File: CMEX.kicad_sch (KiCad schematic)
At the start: 8 parts, among them U1 DAC63004RTET, U2 TPS62151, U3 ADS8584S, U4 TLV8802, U5 TLV8801, U6 LMC7660, U7 SN65MLVD047AD

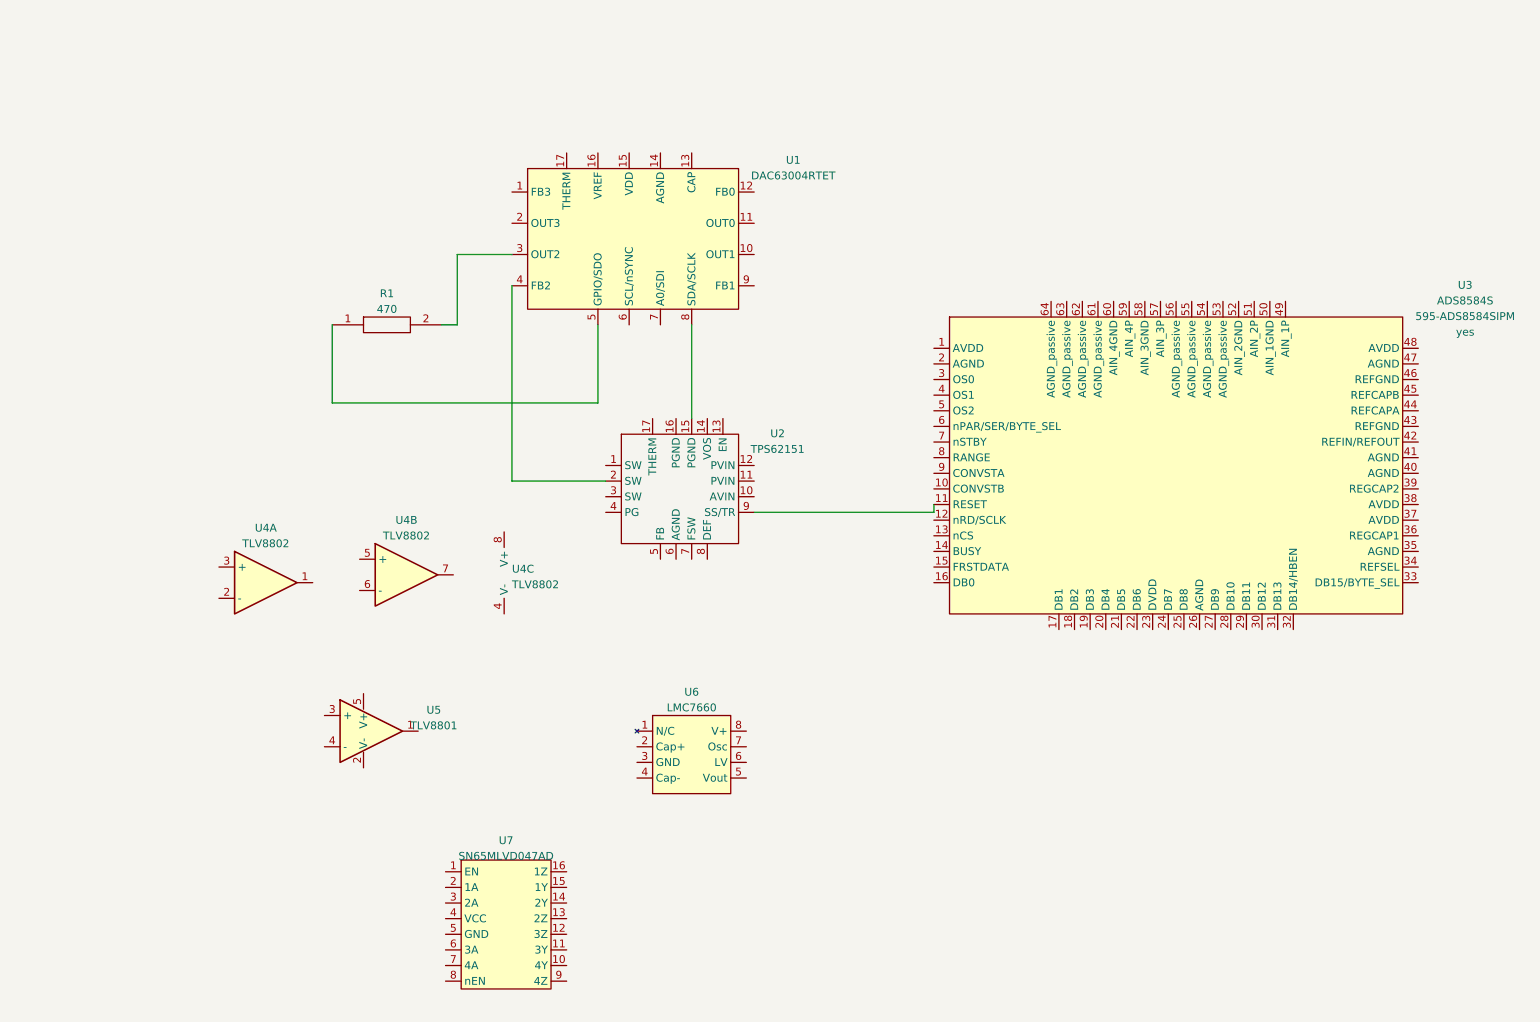
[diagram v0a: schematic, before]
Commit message: Added two sub-sheets for power supply and adc. Started to make the power supply.
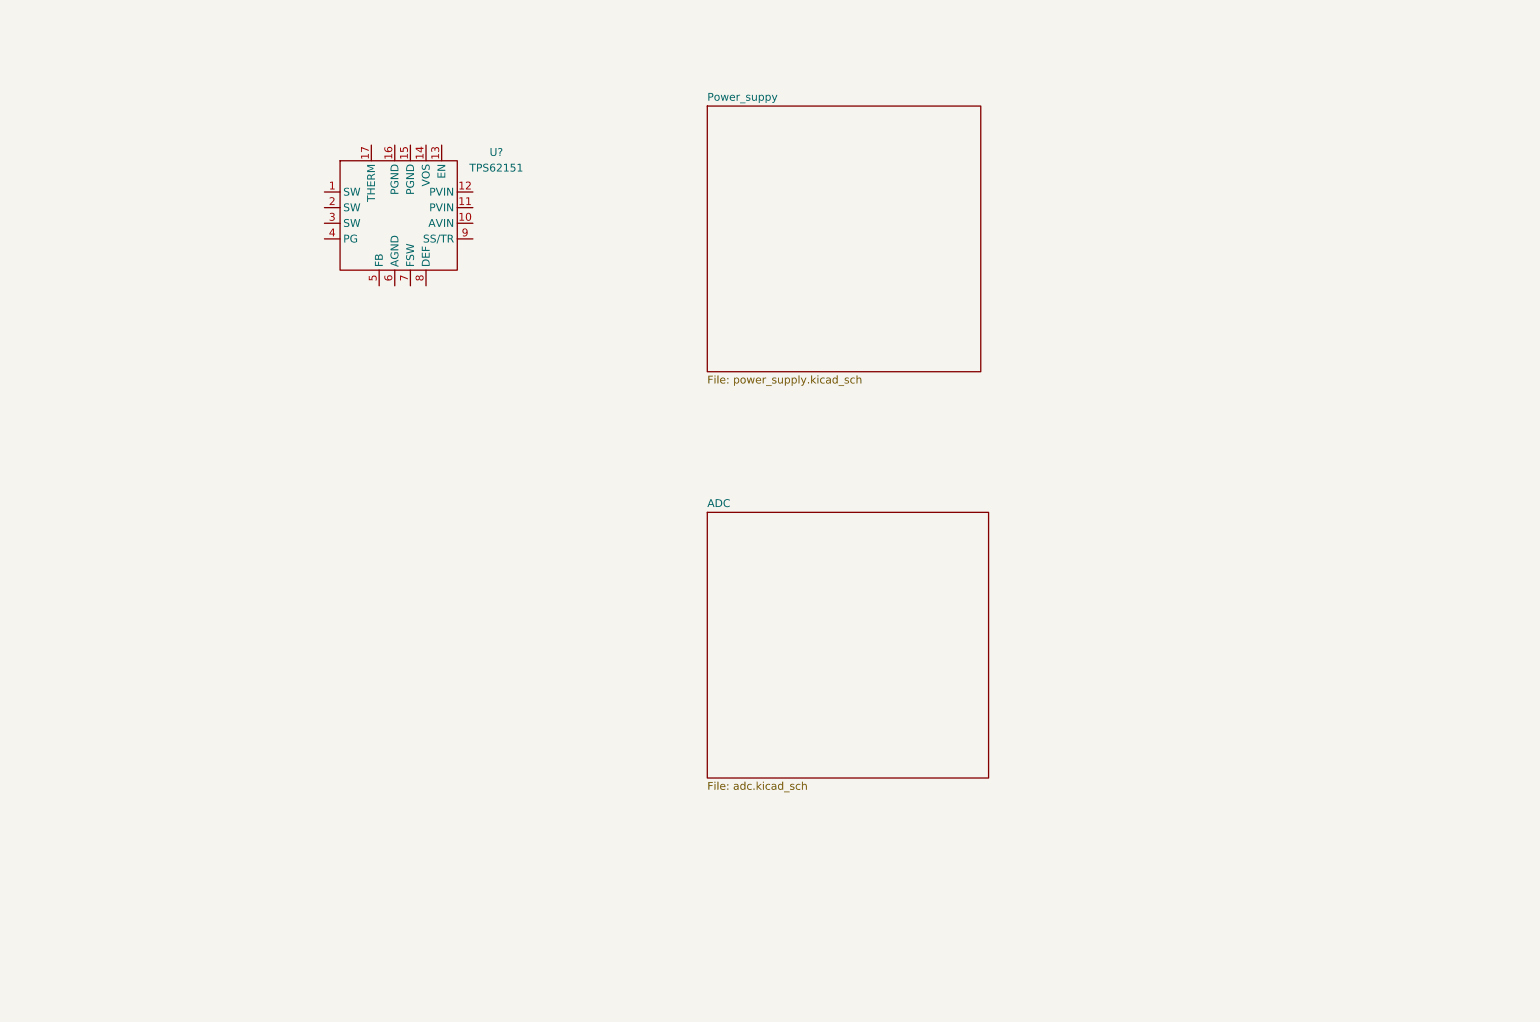
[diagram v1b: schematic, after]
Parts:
- removed R1: R0603_470, Resistor_SMD:R_0603_1608Metric, symbol Jojo_Kicad_Lib:R0603_470
- removed U1: DAC63004RTET, Package_DFN_QFN:WQFN-16-1EP_3x3mm_P0.5mm_EP1.68x1.68mm, symbol Jojo_Kicad_Lib:DAC63004RTET
- removed U2: TPS62151, Package_DFN_QFN:VQFN-16-1EP_3x3mm_P0.5mm_EP1.68x1.68mm, symbol Jojo_Kicad_Lib:TPS62151
- removed U3: ADS8584S, Package_QFP:LQFP-64_10x10mm_P0.5mm, symbol Jojo_Kicad_Lib:ADS8584S
- removed U4: TLV8802, Package_SO:VSSOP-8_3.0x3.0mm_P0.65mm, symbol Jojo_Kicad_Lib:TLV8802
- removed U5: TLV8801, Package_TO_SOT_SMD:SOT-23-5, symbol Jojo_Kicad_Lib:TLV8801
- removed U6: LMC7660, Package_SO:SOIC-8_3.9x4.9mm_P1.27mm, symbol Jojo_Kicad_Lib:LMC7660
- removed U7: SN65MLVD047AD, Package_SO:SOIC-16_3.9x9.9mm_P1.27mm, symbol Jojo_Kicad_Lib:SN65MLVD047AD
- added U?: TPS62151, Package_DFN_QFN:VQFN-16-1EP_3x3mm_P0.5mm_EP1.68x1.68mm, symbol Jojos_Lib:TPS62151
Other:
- added sheet ADC (adc.kicad_sch)
- added sheet Power_suppy (power_supply.kicad_sch)

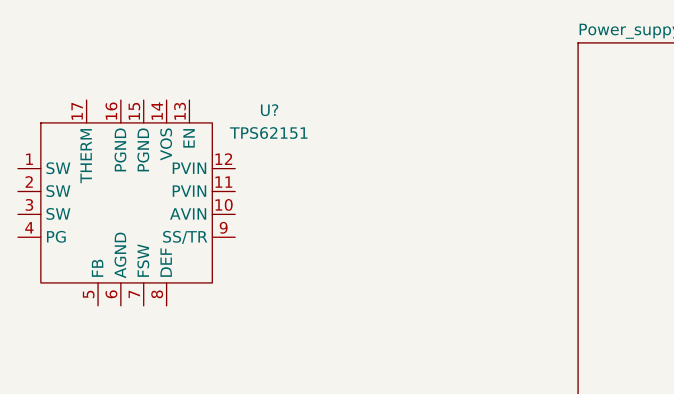
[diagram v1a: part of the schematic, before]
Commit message: Schaltplan für Spannungsversorgung angelegt.
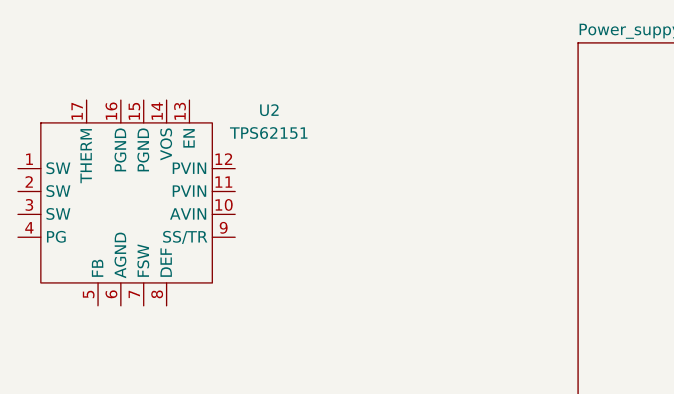
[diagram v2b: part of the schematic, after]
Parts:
- gave numbers to parts that had none: 1
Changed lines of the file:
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@@
   (symbol (lib_id "Jojos_Lib:TPS62151") (at 97.79 60.96 0) (unit 1)
     (in_bom yes) (on_board yes) (dnp no) (fields_autoplaced)
-    (property "Reference" "U?" (at 113.03 49.4283 0)
+    (property "Reference" "U2" (at 113.03 49.4283 0)
       (effects (font (size 1.27 1.27)))
     )
@@
       (project "CMEX"
         (path "/03c4a148-37f4-4d5a-ada3-efb0d725ba7b"
-          (reference "U?") (unit 1)
+          (reference "U2") (unit 1)
         )
       )

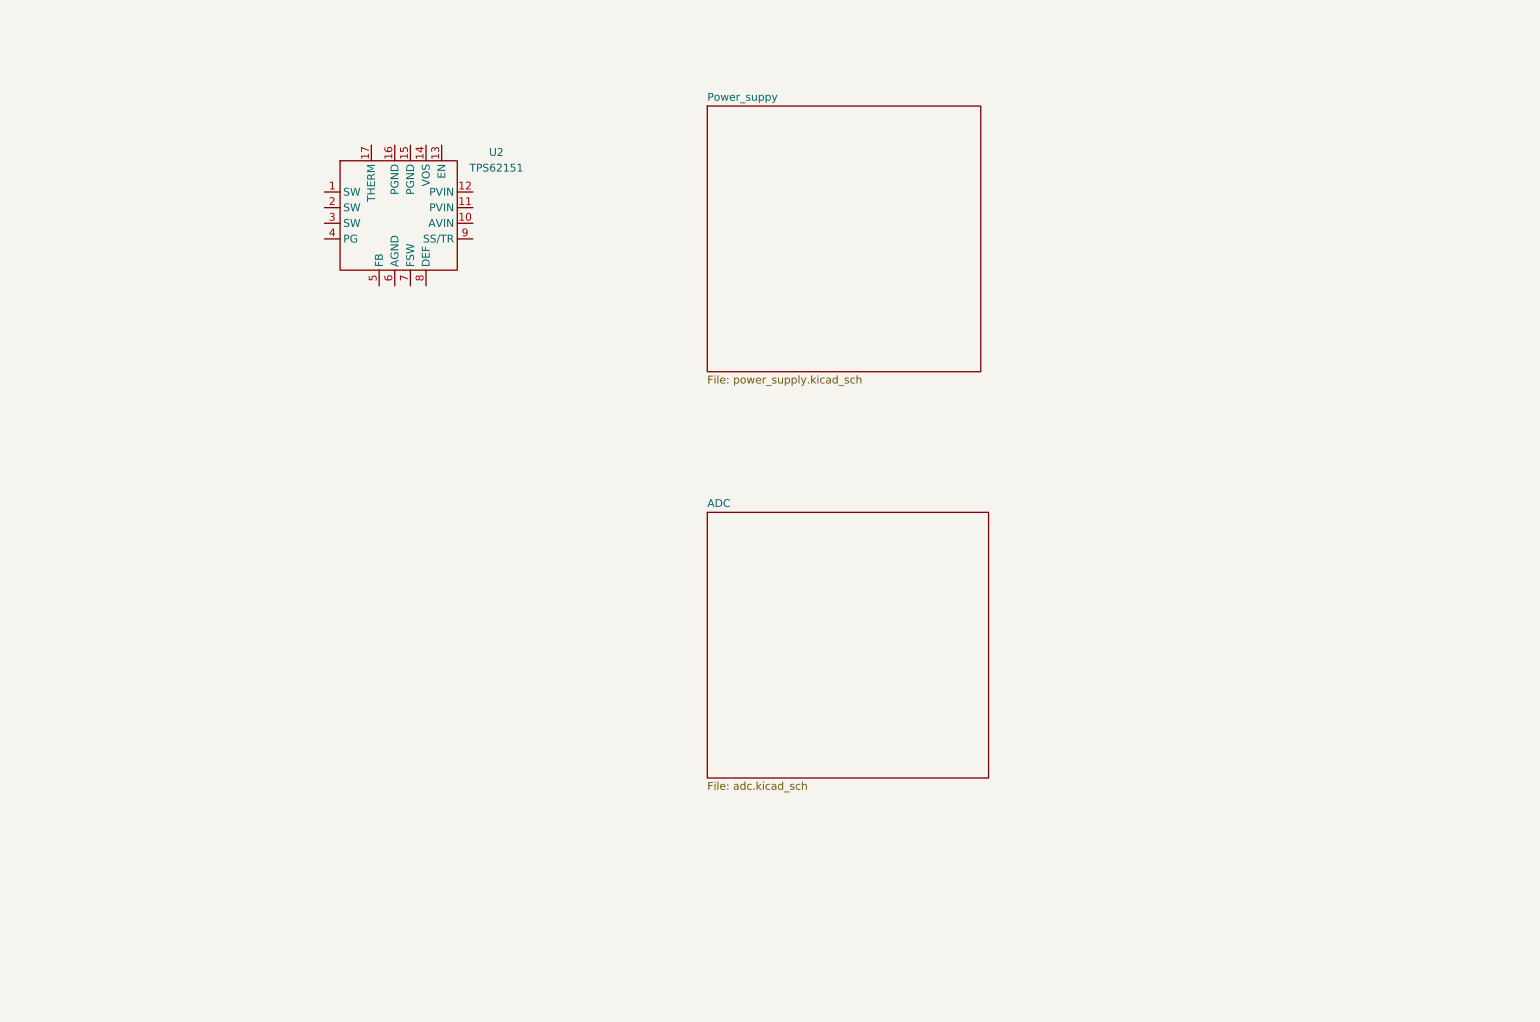
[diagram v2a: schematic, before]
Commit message: Added awags and dac sheet.
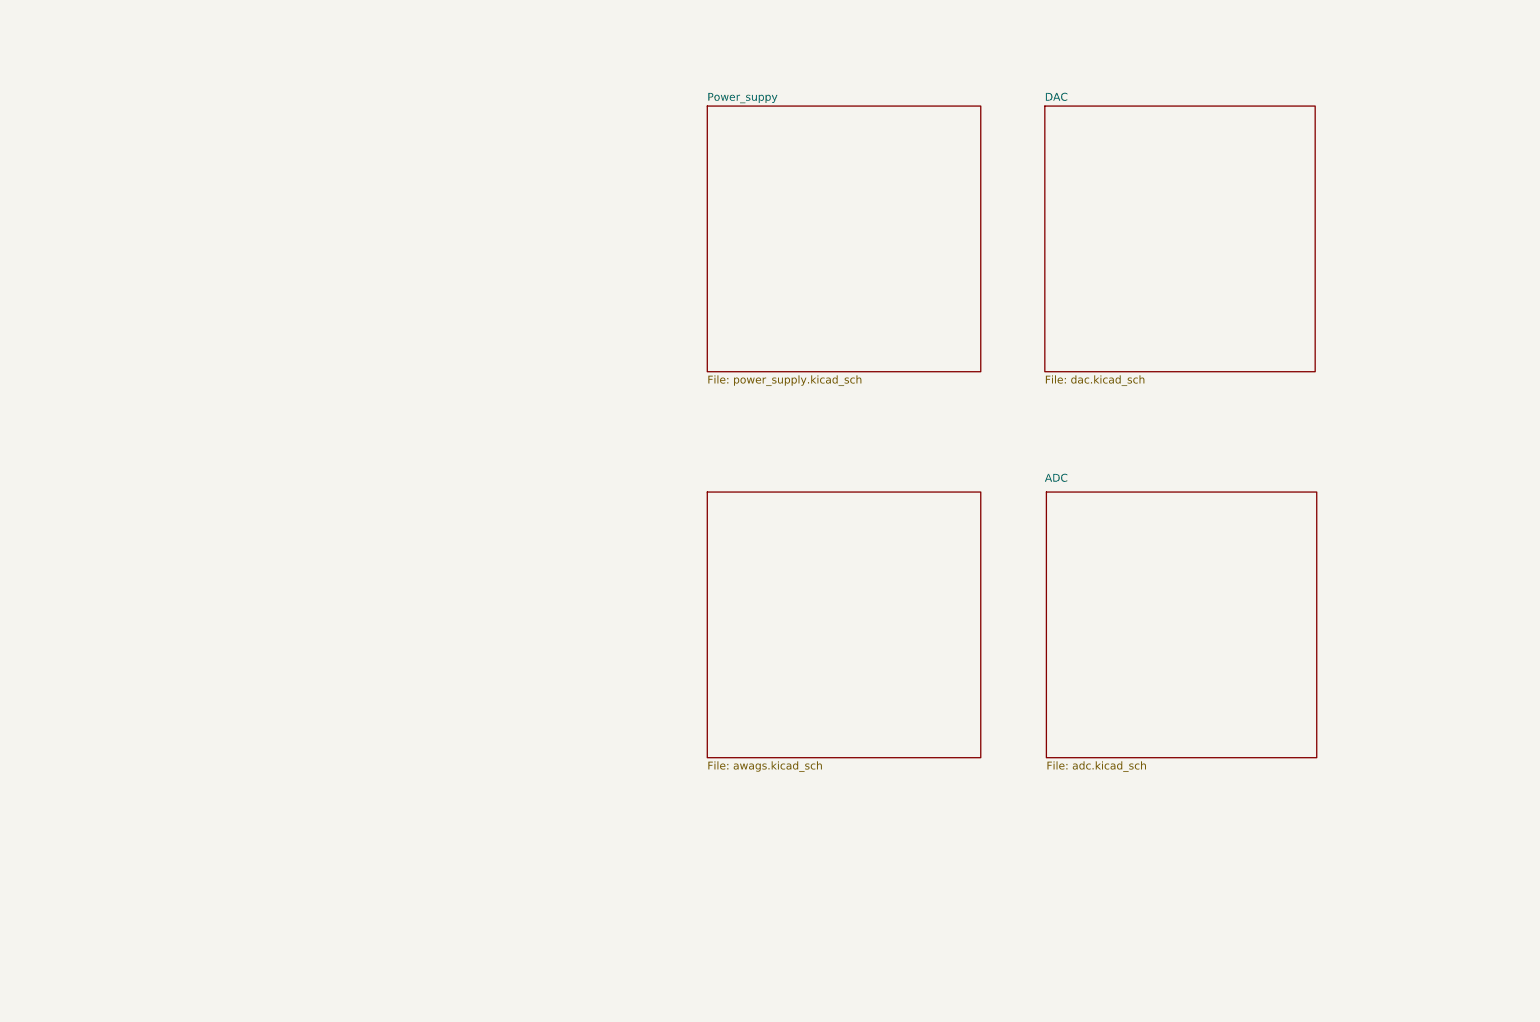
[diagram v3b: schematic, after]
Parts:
- removed U2: TPS62151, Package_DFN_QFN:VQFN-16-1EP_3x3mm_P0.5mm_EP1.68x1.68mm, symbol Jojos_Lib:TPS62151
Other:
- added sheet AWAGS (awags.kicad_sch)
- added sheet DAC (dac.kicad_sch)
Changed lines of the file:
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@@
 (kicad_sch (version 20230121) (generator eeschema)
   (paper "A4")
-  (symbol (lib_id "Jojos_Lib:TPS62151") (at 97.79 60.96 0) (unit 1)
-    (in_bom yes) (on_board yes) (dnp no) (fields_autoplaced)
-    (property "Reference" "U2" (at 113.03 49.4283 0)
-      (effects (font (size 1.27 1.27)))
-    )
-    (property "Value" "TPS62151" (at 113.03 51.9683 0)
-      (effects (font (size 1.27 1.27)))
-    )
-    (property "Footprint" "Package_DFN_QFN:VQFN-16-1EP_3x3mm_P0.5mm_EP1.68x1.68mm" (at 100.33 66.04 0)
-      (effects (font (size 1.27 1.27)) hide)
-    )
-    (property "Datasheet" "" (at 100.33 66.04 0)
-      (effects (font (size 1.27 1.27)) hide)
-    )
-    (property "Mouser Part Number" "595-TPS62150RGTR " (at 97.79 60.96 0)
-      (effects (font (size 1.27 1.27)) hide)
-    )
-    (property "Place" "yes" (at 97.79 60.96 0)
-      (effects (font (size 1.27 1.27)) hide)
-    )
-    (pin "1")
-    (pin "10")
-    (pin "11")
-    (pin "12")
-    (pin "13")
-    (pin "14")
-    (pin "15")
-    (pin "16")
-    (pin "17")
-    (pin "2")
-    (pin "3")
-    (pin "4")
-    (pin "5")
-    (pin "6")
-    (pin "7")
-    (pin "8")
-    (pin "9")
-    (instances
-      (project "CMEX"
-        (path "/03c4a148-37f4-4d5a-ada3-efb0d725ba7b"
-          (reference "U2") (unit 1)
-        )
-      )
-    )
-  )
-  (sheet (at 147.32 107.95) (size 45.72 43.18) (fields_autoplaced)
+  (sheet (at 202.438 104.648) (size 43.942 43.18)
     (stroke (width 0.1524) (type solid))
     (fill (color 0 0 0 0.0000))
-    (property "Sheetname" "ADC" (at 147.32 107.2384 0)
+    (property "Sheetname" "ADC" (at 202.184 103.124 0)
       (effects (font (size 1.27 1.27)) (justify left bottom))
     )
-    (property "Sheetfile" "adc.kicad_sch" (at 147.32 151.7146 0)
+    (property "Sheetfile" "adc.kicad_sch" (at 202.438 148.4126 0)
       (effects (font (size 1.27 1.27)) (justify left top))
     )
@@
       (project "CMEX"
         (path "/03c4a148-37f4-4d5a-ada3-efb0d725ba7b" (page "3"))
+      )
+    )
+  )
+  (sheet (at 202.184 41.91) (size 43.942 43.18) (fields_autoplaced)
+    (stroke (width 0.1524) (type solid))
+    (fill (color 0 0 0 0.0000))
+    (property "Sheetname" "DAC" (at 202.184 41.1984 0)
+      (effects (font (size 1.27 1.27)) (justify left bottom))
+    )
+    (property "Sheetfile" "dac.kicad_sch" (at 202.184 85.6746 0)
+      (effects (font (size 1.27 1.27)) (justify left top))
+    )
+    (instances
+      (project "CMEX"
+        (path "/03c4a148-37f4-4d5a-ada3-efb0d725ba7b" (page "5"))
       )
     )
@@
       )
     )
+  )
+  (sheet (at 147.32 104.648) (size 44.45 43.18) (fields_autoplaced)
+    (stroke (width 0.1524) (type solid))
+    (fill (color 0 0 0 0.0000))
+    (property "Sheetname" "AWAGS" (at 147.32 103.9364 0)
+      (effects (font (size 1.27 1.27)) (justify left bottom) hide)
+    )
+    (property "Sheetfile" "awags.kicad_sch" (at 147.32 148.4126 0)
+      (effects (font (size 1.27 1.27)) (justify left top))
+    )
+    (instances
+      (project "CMEX"
+        (path "/03c4a148-37f4-4d5a-ada3-efb0d725ba7b" (page "4"))
+      )
+    )

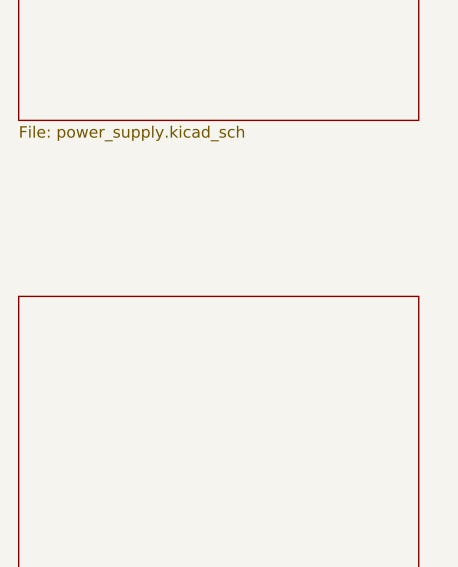
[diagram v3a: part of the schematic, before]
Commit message: Added DAC circuit.
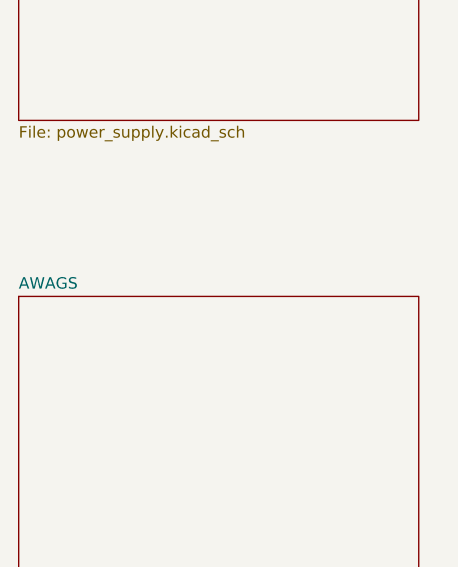
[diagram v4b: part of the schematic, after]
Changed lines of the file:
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@@
     (fill (color 0 0 0 0.0000))
     (property "Sheetname" "AWAGS" (at 147.32 103.9364 0)
-      (effects (font (size 1.27 1.27)) (justify left bottom) hide)
+      (effects (font (size 1.27 1.27)) (justify left bottom))
     )
     (property "Sheetfile" "awags.kicad_sch" (at 147.32 148.4126 0)
